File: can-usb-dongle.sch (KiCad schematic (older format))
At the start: 31 parts

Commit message: note differnt possible CAN transceivers.
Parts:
- D?: value LED -> CAN1
- D?: value LED -> CAN2
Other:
- note added: "ST L99616\nTI SN65HVD256\nMAX3051\nLT1796\n"
- note removed: "ST L99616"
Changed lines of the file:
@@
 $EndComp
 Text Notes 8950 2700 0    50   ~ 0
-ST L99616
+ST L99616\nTI SN65HVD256\nMAX3051\nLT1796\n
 $Comp
 L STM32F105RBT6 U?
@@
 P 10000 1950
 F 0 "D?" H 10000 2050 50  0000 C CNN
-F 1 "LED" H 10000 1850 50  0000 C CNN
+F 1 "CAN1" H 10000 1850 50  0000 C CNN
 F 2 "" H 10000 1950 60  0000 C CNN
 F 3 "" H 10000 1950 60  0000 C CNN
@@
 P 10000 3450
 F 0 "D?" H 10000 3550 50  0000 C CNN
-F 1 "LED" H 10000 3350 50  0000 C CNN
+F 1 "CAN2" H 10000 3350 50  0000 C CNN
 F 2 "" H 10000 3450 60  0000 C CNN
 F 3 "" H 10000 3450 60  0000 C CNN

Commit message: Switch to STM32F3 LQFP48 with only 1 CAN interface.
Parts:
- removed CONN?: CAN2, MODULE, symbol CAN
- removed D?: CAN2, symbol LED
- removed R?: 10k, symbol R
- removed R?: R, symbol R
- removed U?: STM32F105RBT6, MODULE, symbol STM32F105RBT6
- added CONN?: MICRO_USB, symbol MICRO_USB
- added CONN?: CAN1, MODULE, symbol CAN
- added R?: 47k, symbol R
- added R?: 1.5k, symbol R
- added U?: STM32F302C8T, MODULE, symbol STM32F302C8T
- added U?: SN65HVD256, MODULE, symbol SN65HVD256
- X?: value 8MHz 10ppm -> 16MHz 10ppm
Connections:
- net labels added: BUTTON, CAN_SILENT, STATUS_LED, UART1_RX, UART1_TX
- net labels removed: CAN2_LED, CAN2_RX, CAN2_TX, UART4_RX, UART4_TX
- wire segments 65 -> 74
- no-connect marks 4 -> 3
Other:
- note added: "(*)"
- note added: "(*) needed for USB dfu bootloader"
- note added: "press button for dfu bootloader"
- note added: "see AN2606\nSTM32F302x8\nBootloader configuration"
- note removed: "BOOT1 low:\nflash app or bootloader"
- note removed: "ST L99616\nTI SN65HVD256\nMAX3051\nLT1796\n"
- moved on the sheet: C?, CONN?, D?, P?, R?, SW?, X?

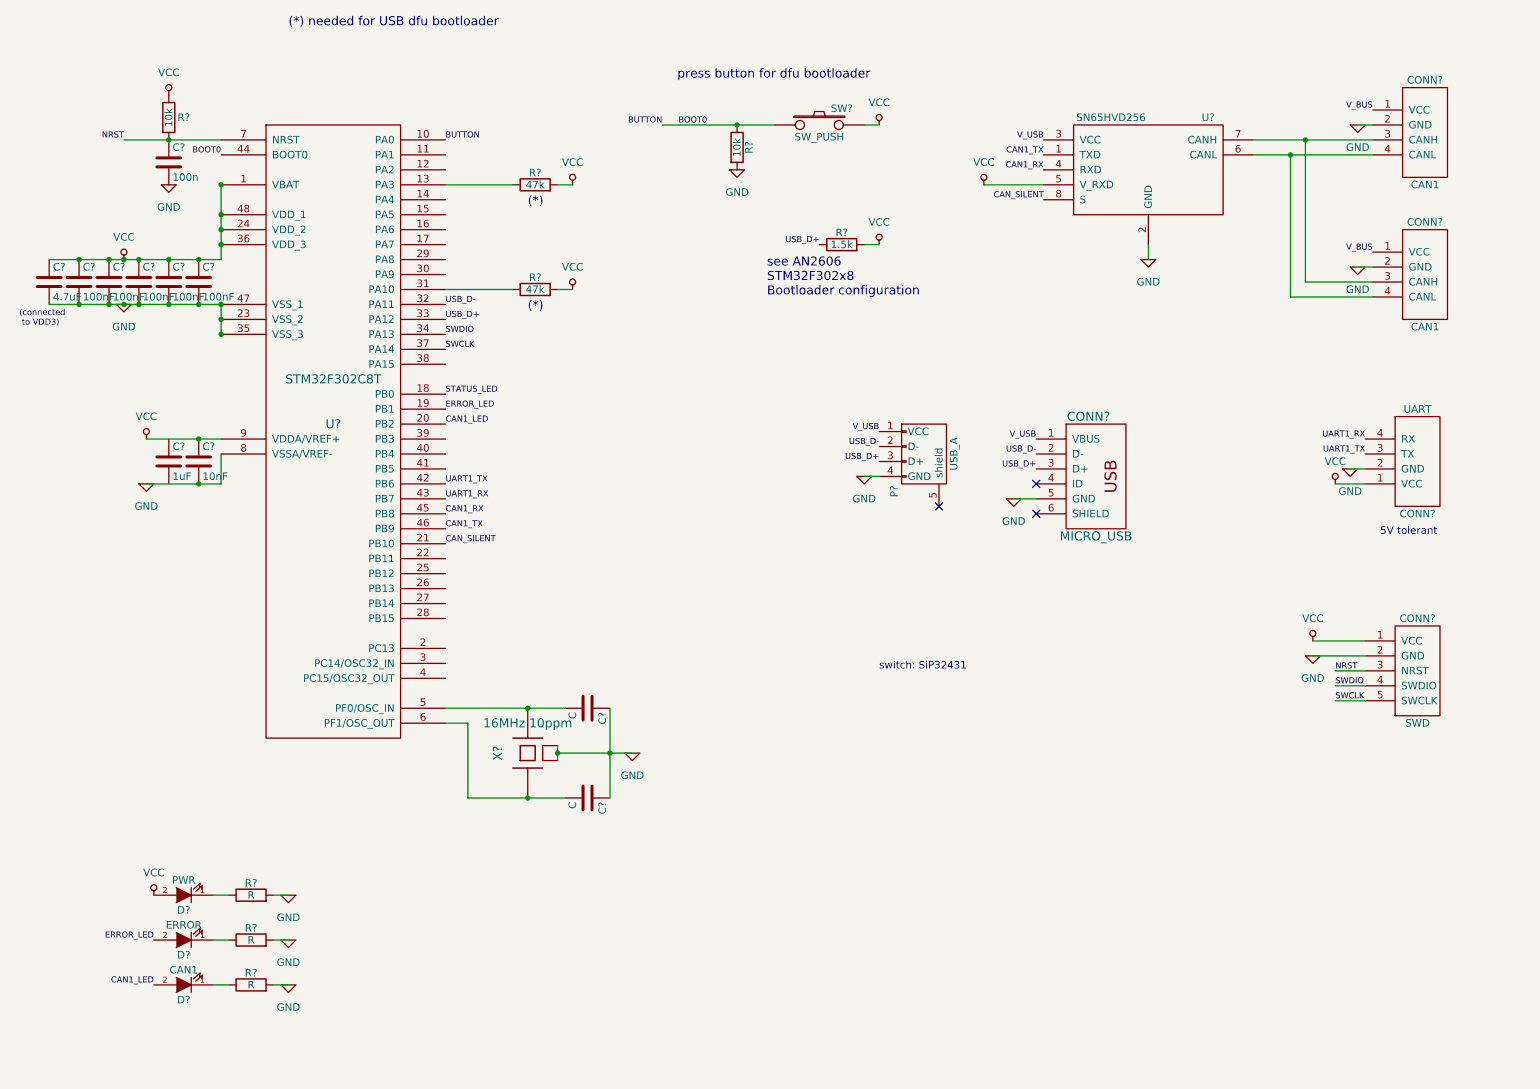
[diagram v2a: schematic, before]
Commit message: Changes to reduce cost.
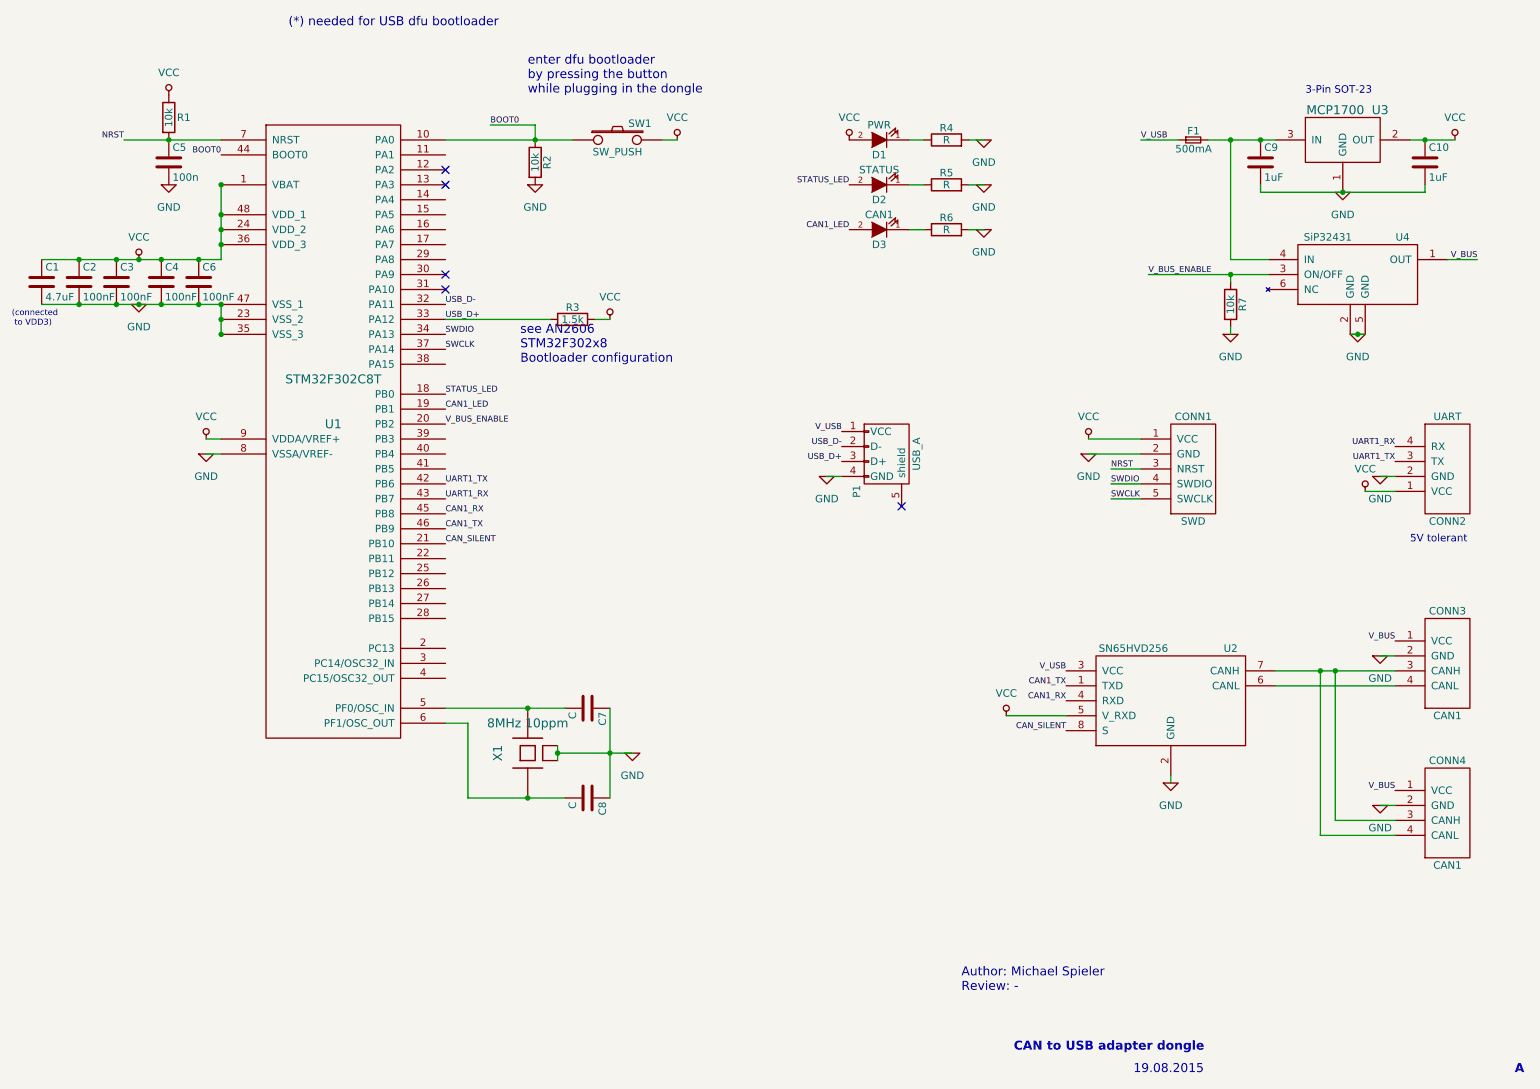
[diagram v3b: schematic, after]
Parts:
- removed C?: 100nF, symbol C
- removed C?: 10nF, symbol C
- removed C?: 1uF, symbol C
- removed CONN?: MICRO_USB, symbol MICRO_USB
- removed CONN?: CAN1, MODULE, symbol CAN
- removed R? (x2): 47k, symbol R
- added C10, C9: 1uF, Capacitors_SMD:C_0603_HandSoldering, symbol C
- added CONN4: CAN1, Connectors_Molex:Connector_Molex_PicoBlade_53261-0471, symbol CAN
- added F1: 500mA, Resistors_SMD:R_0805_HandSoldering, symbol F_Small
- added R7: 10k, Resistors_SMD:R_0603, symbol R
- added U3: MCP1700, Housings_SOT-23_SOT-143_TSOT-6:SOT-23, symbol MCP1700
- added U4: SiP32431, symbol SiP32431
- C1, C2, C3, C4, C5, C6, C7, C8: renamed from C?; footprint (none) -> Capacitors_SMD:C_0603_HandSoldering
- CONN1, CONN2: renamed from CONN?; footprint MODULE -> (none)
- CONN3: renamed from CONN?; footprint MODULE -> Connectors_Molex:Connector_Molex_PicoBlade_53261-0471
- D1, D3: renamed from D?; footprint (none) -> LEDs:LED-0603
- D2: renamed from D?; value ERROR -> STATUS; footprint (none) -> LEDs:LED-0603
- R1, R2, R3, R4, R5, R6: renamed from R?; footprint (none) -> Resistors_SMD:R_0603
- U1: renamed from U?; footprint MODULE -> Housings_QFP:LQFP-48_7x7mm_Pitch0.5mm
- U2: renamed from U?; footprint MODULE -> Transistors_SMD:sc70-5
- X1: renamed from X?; value 16MHz 10ppm -> 8MHz 10ppm
- gave numbers to parts that had none: 2
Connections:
- net CAN1_LED: now also U1.19 (PB1); no longer U1.20 (PB2)
- net GND: now also C10.2, C9.2, CONN4.2 (GND), CONN4.MECH (GND), R7.2, U3.1 (GND), U4.2 (GND), U4.5 (GND)
- net STATUS_LED: now also D2.2 (A)
- net VCC: now also C10.1, U3.2 (OUT)
- net V_BUS: now also CONN4.1 (VCC), U4.1 (OUT)
- net V_USB: now also F1.1
- net at CONN3.3 (CANH), U2.7 (CANH): now also CONN4.3 (CANH), CONN4.4 (CANL)
- removed net ERROR_LED: D2.2 (A), U1.19 (PB1)
- new net: C9.1, F1.2, U3.3 (IN), U4.4 (IN)
- new net V_BUS_ENABLE: R7.1, U1.20 (PB2), U4.3 (ON/OFF)
- no-connect marks 3 -> 5
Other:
- note added: "19.08.2015"
- note added: "3-Pin SOT-23"
- note added: "A"
- note added: "Author: Michael Spieler\nReview: -"
- note added: "CAN to USB adapter dongle"
- note added: "enter dfu bootloader\nby pressing the button\nwhile plugging in the dongle"
- note removed: "(*)"
- note removed: "press button for dfu bootloader"
- note removed: "switch: SiP32431"
- moved on the sheet: C1, C3, C4, C6, CONN1, CONN2, CONN3, D1, D2, D3, P1, R2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

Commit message: start assigning footprints.
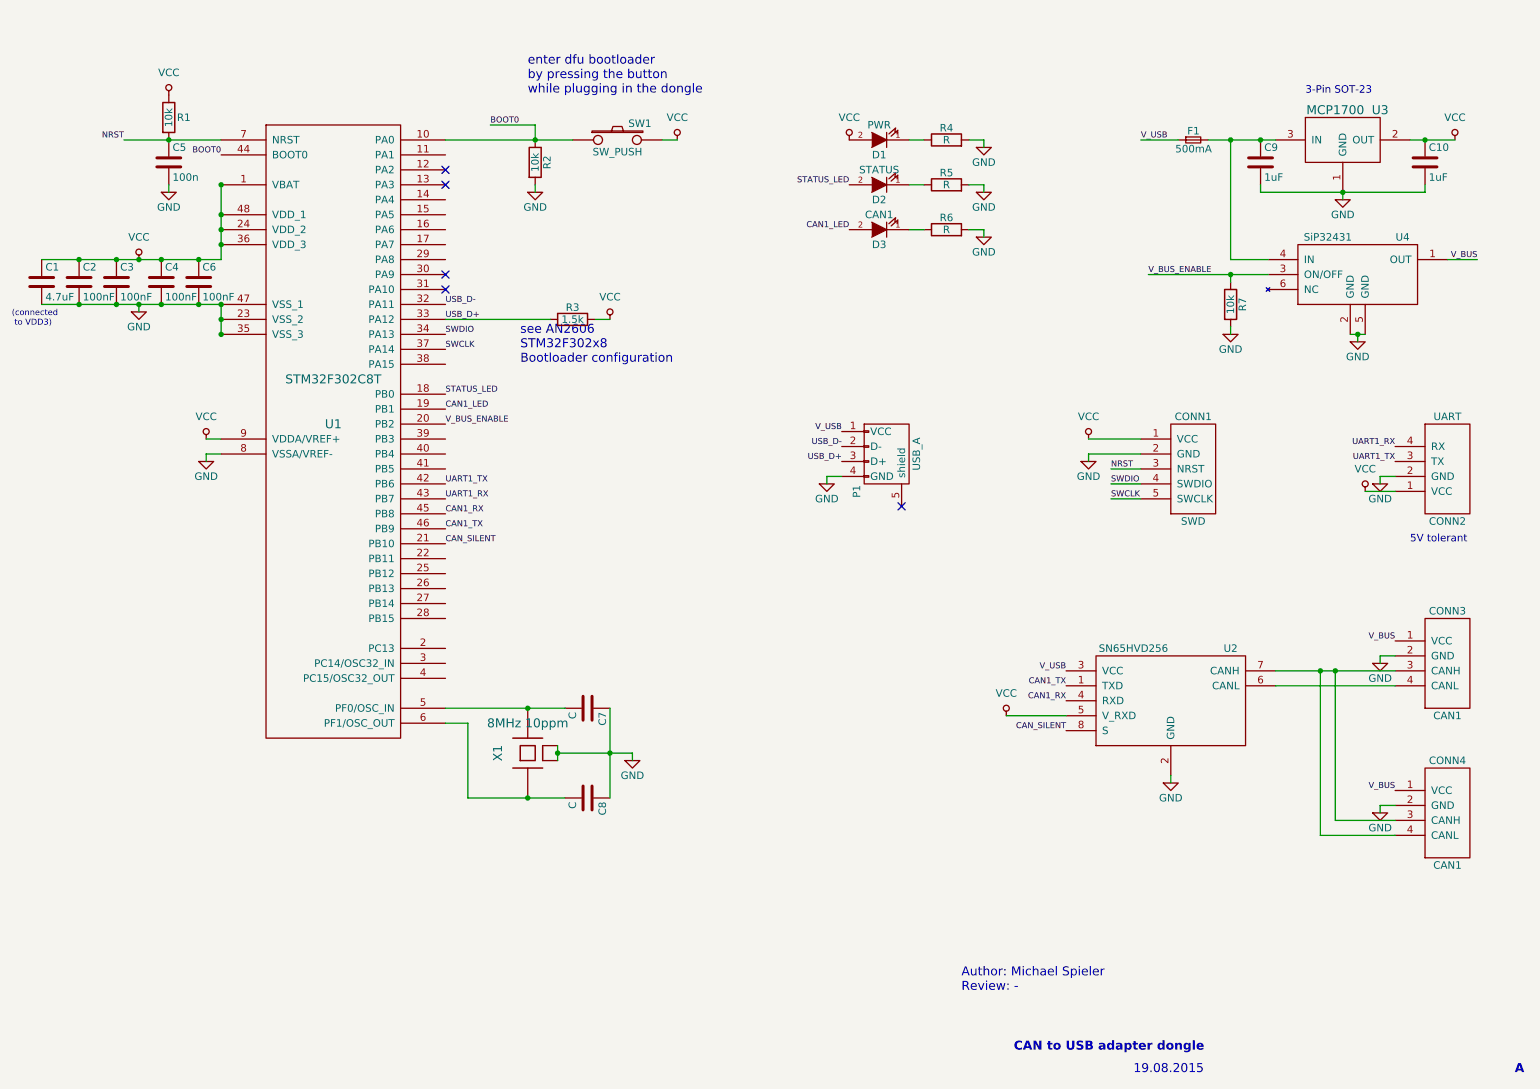
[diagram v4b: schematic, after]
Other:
- note removed: "(*) needed for USB dfu bootloader"
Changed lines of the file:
@@
 EESchema Schematic File Version 2
+LIBS:can-usb-dongle-rescue
 LIBS:power
 LIBS:device
@@
 L GND #PWR01
 U 1 1 5561F00A
-P 1550 2500
-F 0 "#PWR01" H 1550 2250 50  0001 C CNN
-F 1 "GND" H 1550 2350 50  0000 C CNN
-F 2 "" H 1550 2500 60  0000 C CNN
-F 3 "" H 1550 2500 60  0000 C CNN
-	1    1550 2500
+P 1550 2550
+F 0 "#PWR01" H 1550 2300 50  0001 C CNN
+F 1 "GND" H 1550 2450 50  0000 C CNN
+F 2 "" H 1550 2550 60  0000 C CNN
+F 3 "" H 1550 2550 60  0000 C CNN
+	1    1550 2550
 	1    0    0    -1
 $EndComp
@@
 L GND #PWR03
 U 1 1 5561F50D
-P 2000 3500
-F 0 "#PWR03" H 2000 3250 50  0001 C CNN
-F 1 "GND" H 2000 3350 50  0000 C CNN
-F 2 "" H 2000 3500 60  0000 C CNN
-F 3 "" H 2000 3500 60  0000 C CNN
-	1    2000 3500
+P 2000 3550
+F 0 "#PWR03" H 2000 3300 50  0001 C CNN
+F 1 "GND" H 2000 3450 50  0000 C CNN
+F 2 "" H 2000 3550 60  0000 C CNN
+F 3 "" H 2000 3550 60  0000 C CNN
+	1    2000 3550
 	1    0    0    -1
 $EndComp
@@
 L GND #PWR06
 U 1 1 556206EF
-P 7900 3500
-F 0 "#PWR06" H 7900 3250 50  0001 C CNN
-F 1 "GND" H 7900 3350 50  0000 C CNN
-F 2 "" H 7900 3500 60  0000 C CNN
-F 3 "" H 7900 3500 60  0000 C CNN
-	1    7900 3500
+P 7900 3550
+F 0 "#PWR06" H 7900 3300 50  0001 C CNN
+F 1 "GND" H 7900 3450 50  0000 C CNN
+F 2 "" H 7900 3550 60  0000 C CNN
+F 3 "" H 7900 3550 60  0000 C CNN
+	1    7900 3550
 	1    0    0    -1
 $EndComp
@@
 L GND #PWR08
 U 1 1 556213D3
-P 4850 5500
-F 0 "#PWR08" H 4850 5250 50  0001 C CNN
-F 1 "GND" H 4850 5350 50  0000 C CNN
-F 2 "" H 4850 5500 60  0000 C CNN
-F 3 "" H 4850 5500 60  0000 C CNN
-	1    4850 5500
+P 4850 5550
+F 0 "#PWR08" H 4850 5300 50  0001 C CNN
+F 1 "GND" H 4850 5450 50  0000 C CNN
+F 2 "" H 4850 5550 60  0000 C CNN
+F 3 "" H 4850 5550 60  0000 C CNN
+	1    4850 5550
 	1    0    0    -1
 $EndComp
@@
 L GND #PWR09
 U 1 1 55621D6C
-P 6150 3650
-F 0 "#PWR09" H 6150 3400 50  0001 C CNN
-F 1 "GND" H 6150 3500 50  0000 C CNN
-F 2 "" H 6150 3650 60  0000 C CNN
-F 3 "" H 6150 3650 60  0000 C CNN
-	1    6150 3650
+P 6150 3700
+F 0 "#PWR09" H 6150 3450 50  0001 C CNN
+F 1 "GND" H 6150 3600 50  0000 C CNN
+F 2 "" H 6150 3700 60  0000 C CNN
+F 3 "" H 6150 3700 60  0000 C CNN
+	1    6150 3700
 	1    0    0    -1
 $EndComp
@@
 L GND #PWR010
 U 1 1 5562325F
-P 1750 1700
-F 0 "#PWR010" H 1750 1450 50  0001 C CNN
-F 1 "GND" H 1750 1550 50  0000 C CNN
-F 2 "" H 1750 1700 60  0000 C CNN
-F 3 "" H 1750 1700 60  0000 C CNN
-	1    1750 1700
+P 1750 1750
+F 0 "#PWR010" H 1750 1500 50  0001 C CNN
+F 1 "GND" H 1750 1650 50  0000 C CNN
+F 2 "" H 1750 1750 60  0000 C CNN
+F 3 "" H 1750 1750 60  0000 C CNN
+	1    1750 1750
 	1    0    0    -1
 $EndComp
@@
 L GND #PWR011
 U 1 1 55623201
-P 7200 2000
-F 0 "#PWR011" H 7200 1750 50  0001 C CNN
-F 1 "GND" H 7200 1850 50  0000 C CNN
-F 2 "" H 7200 2000 60  0000 C CNN
-F 3 "" H 7200 2000 60  0000 C CNN
-	1    7200 2000
+P 7200 2050
+F 0 "#PWR011" H 7200 1800 50  0001 C CNN
+F 1 "GND" H 7200 1950 50  0000 C CNN
+F 2 "" H 7200 2050 60  0000 C CNN
+F 3 "" H 7200 2050 60  0000 C CNN
+	1    7200 2050
 	1    0    0    -1
 $EndComp
@@
 L GND #PWR012
 U 1 1 55624280
-P 7200 1700
-F 0 "#PWR012" H 7200 1450 50  0001 C CNN
-F 1 "GND" H 7200 1550 50  0000 C CNN
-F 2 "" H 7200 1700 60  0000 C CNN
-F 3 "" H 7200 1700 60  0000 C CNN
-	1    7200 1700
+P 7200 1750
+F 0 "#PWR012" H 7200 1500 50  0001 C CNN
+F 1 "GND" H 7200 1650 50  0000 C CNN
+F 2 "" H 7200 1750 60  0000 C CNN
+F 3 "" H 7200 1750 60  0000 C CNN
+	1    7200 1750
 	1    0    0    -1
 $EndComp
@@
 L GND #PWR013
 U 1 1 55624C2B
-P 4200 1700
-F 0 "#PWR013" H 4200 1450 50  0001 C CNN
-F 1 "GND" H 4200 1550 50  0000 C CNN
-F 2 "" H 4200 1700 60  0000 C CNN
-F 3 "" H 4200 1700 60  0000 C CNN
-	1    4200 1700
+P 4200 1750
+F 0 "#PWR013" H 4200 1500 50  0001 C CNN
+F 1 "GND" H 4200 1650 50  0000 C CNN
+F 2 "" H 4200 1750 60  0000 C CNN
+F 3 "" H 4200 1750 60  0000 C CNN
+	1    4200 1750
 	1    0    0    -1
 $EndComp
@@
 L GND #PWR015
 U 1 1 55624F8A
-P 7200 1400
-F 0 "#PWR015" H 7200 1150 50  0001 C CNN
-F 1 "GND" H 7200 1250 50  0000 C CNN
-F 2 "" H 7200 1400 60  0000 C CNN
-F 3 "" H 7200 1400 60  0000 C CNN
-	1    7200 1400
+P 7200 1450
+F 0 "#PWR015" H 7200 1200 50  0001 C CNN
+F 1 "GND" H 7200 1350 50  0000 C CNN
+F 2 "" H 7200 1450 60  0000 C CNN
+F 3 "" H 7200 1450 60  0000 C CNN
+	1    7200 1450
 	1    0    0    -1
 $EndComp
@@
 L GND #PWR017
 U 1 1 55629057
-P 9850 3650
-F 0 "#PWR017" H 9850 3400 50  0001 C CNN
-F 1 "GND" H 9850 3500 50  0000 C CNN
-F 2 "" H 9850 3650 60  0000 C CNN
-F 3 "" H 9850 3650 60  0000 C CNN
-	1    9850 3650
+P 9850 3700
+F 0 "#PWR017" H 9850 3450 50  0001 C CNN
+F 1 "GND" H 9850 3600 50  0000 C CNN
+F 2 "" H 9850 3700 60  0000 C CNN
+F 3 "" H 9850 3700 60  0000 C CNN
+	1    9850 3700
 	1    0    0    -1
 $EndComp
@@
 P 8450 5700
 F 0 "#PWR019" H 8450 5450 50  0001 C CNN
-F 1 "GND" H 8450 5550 50  0000 C CNN
+F 1 "GND" H 8450 5600 50  0000 C CNN
 F 2 "" H 8450 5700 60  0000 C CNN
 F 3 "" H 8450 5700 60  0000 C CNN
@@
 Text Label 7750 5350 2    40   ~ 0
 CAN_SILENT
-Text Notes 2550 650  0    60   ~ 0
-(*) needed for USB dfu bootloader
 $Comp
 L R R3
@@
 L GND #PWR022
 U 1 1 5592D611
-P 9850 4850
-F 0 "#PWR022" H 9850 4600 50  0001 C CNN
-F 1 "GND" H 9850 4700 50  0000 C CNN
-F 2 "" H 9850 4850 60  0000 C CNN
-F 3 "" H 9850 4850 60  0000 C CNN
-	1    9850 4850
+P 9850 4900
+F 0 "#PWR022" H 9850 4650 50  0001 C CNN
+F 1 "GND" H 9850 4800 50  0000 C CNN
+F 2 "" H 9850 4900 60  0000 C CNN
+F 3 "" H 9850 4900 60  0000 C CNN
+	1    9850 4900
 	1    0    0    -1
 $EndComp
@@
 L GND #PWR023
 U 1 1 55D302BE
-P 9600 1750
-F 0 "#PWR023" H 9600 1500 50  0001 C CNN
-F 1 "GND" H 9600 1600 50  0000 C CNN
-F 2 "" H 9600 1750 60  0000 C CNN
-F 3 "" H 9600 1750 60  0000 C CNN
-	1    9600 1750
+P 9600 1800
+F 0 "#PWR023" H 9600 1550 50  0001 C CNN
+F 1 "GND" H 9600 1700 50  0000 C CNN
+F 2 "" H 9600 1800 60  0000 C CNN
+F 3 "" H 9600 1800 60  0000 C CNN
+	1    9600 1800
 	1    0    0    -1
 $EndComp
@@
 L GND #PWR025
 U 1 1 55D31885
-P 9700 2700
-F 0 "#PWR025" H 9700 2450 50  0001 C CNN
-F 1 "GND" H 9700 2550 50  0000 C CNN
-F 2 "" H 9700 2700 60  0000 C CNN
-F 3 "" H 9700 2700 60  0000 C CNN
-	1    9700 2700
+P 9700 2750
+F 0 "#PWR025" H 9700 2500 50  0001 C CNN
+F 1 "GND" H 9700 2650 50  0000 C CNN
+F 2 "" H 9700 2750 60  0000 C CNN
+F 3 "" H 9700 2750 60  0000 C CNN
+	1    9700 2750
 	1    0    0    -1
 $EndComp
@@
 P 8850 2700
 F 0 "#PWR026" H 8850 2450 50  0001 C CNN
-F 1 "GND" H 8850 2550 50  0000 C CNN
+F 1 "GND" H 8850 2600 50  0000 C CNN
 F 2 "" H 8850 2700 60  0000 C CNN
 F 3 "" H 8850 2700 60  0000 C CNN
@@
 L GND #PWR027
 U 1 1 55D47D26
-P 9850 5850
-F 0 "#PWR027" H 9850 5600 50  0001 C CNN
-F 1 "GND" H 9850 5700 50  0000 C CNN
-F 2 "" H 9850 5850 60  0000 C CNN
-F 3 "" H 9850 5850 60  0000 C CNN
-	1    9850 5850
+P 9850 5900
+F 0 "#PWR027" H 9850 5650 50  0001 C CNN
+F 1 "GND" H 9850 5800 50  0000 C CNN
+F 2 "" H 9850 5900 60  0000 C CNN
+F 3 "" H 9850 5900 60  0000 C CNN
+	1    9850 5900
 	1    0    0    -1
 $EndComp
@@
 Text Notes 7050 7100 0    60   ~ 0
 Author: Michael Spieler\nReview: -
+Wire Wire Line
+	4850 5500 4850 5550
+Wire Wire Line
+	9850 3700 9850 3650
+Wire Wire Line
+	9850 4900 9850 4850
+Wire Wire Line
+	9850 5900 9850 5850
+Wire Wire Line
+	9700 2750 9700 2700
+Wire Wire Line
+	9600 1800 9600 1750
+Wire Wire Line
+	7200 2000 7200 2050
+Wire Wire Line
+	7200 1700 7200 1750
+Wire Wire Line
+	7200 1400 7200 1450
+Wire Wire Line
+	4200 1750 4200 1700
+Wire Wire Line
+	1750 1750 1750 1700
+Wire Wire Line
+	1550 2550 1550 2500
+Wire Wire Line
+	2000 3550 2000 3500
+Wire Wire Line
+	6150 3700 6150 3650
+Wire Wire Line
+	7900 3500 7900 3550
 $EndSCHEMATC
